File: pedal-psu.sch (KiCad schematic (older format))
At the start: 89 parts, among them J1 Conn_01x01_Male, J2 Conn_01x01_Male, J3 Power Sockets, J4 LCD Display, J7 Status LEDS, T1 Transformer_1P_1S, T2 Transformer_1P_1S, U1 LM7809_TO220, U2 LM324, U3 LM7809_TO220, U4 LM7805_TO220, U5 LM317_3PinPackage, U6 LM7809_TO220, U7 74HC595

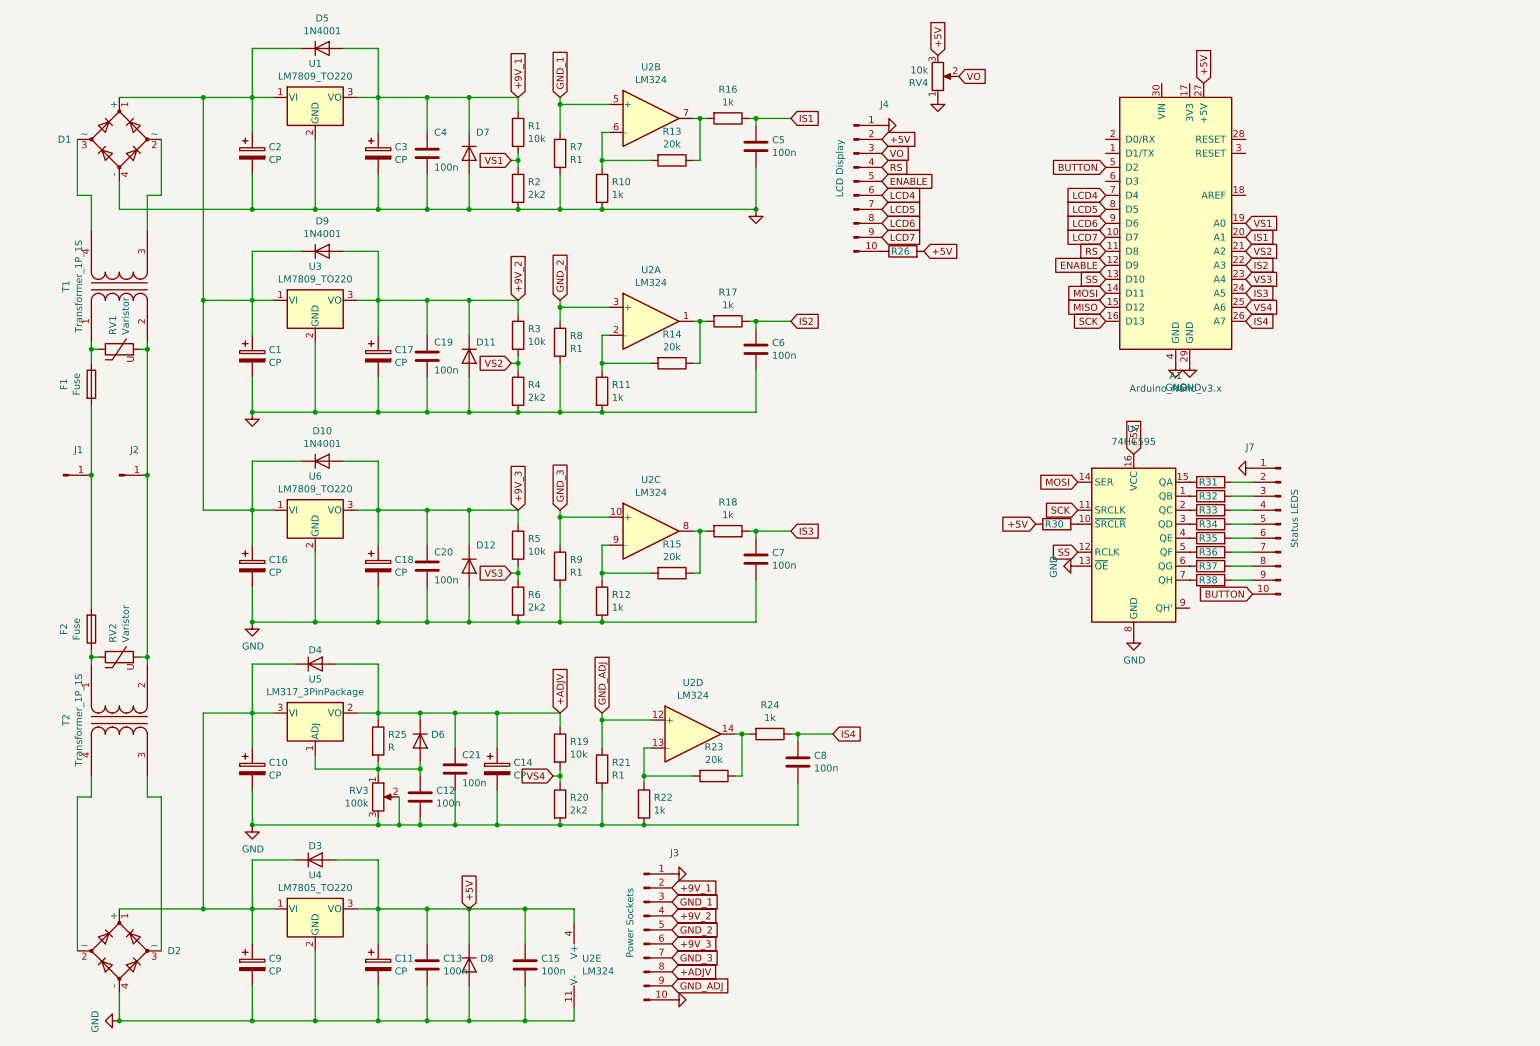
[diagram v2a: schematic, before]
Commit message: Removed 2nd trafo.
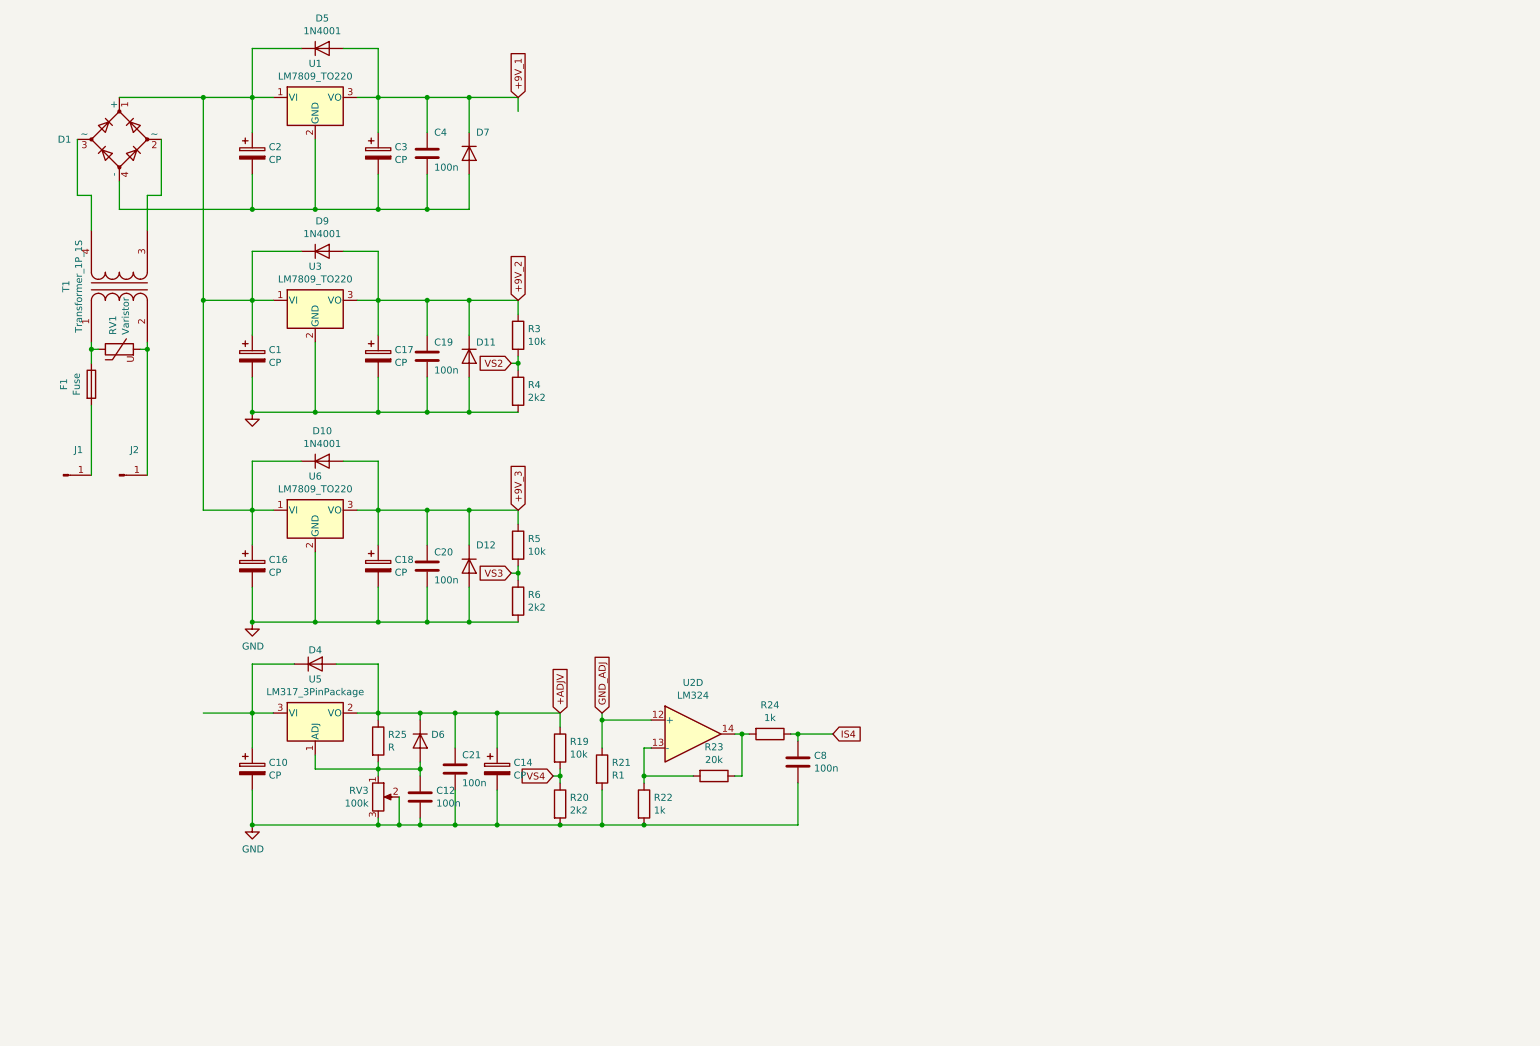
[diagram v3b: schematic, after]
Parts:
- removed A1: Arduino_Nano_v3.x, Module:Arduino_Nano, symbol MCU_Module:Arduino_Nano_v3.x
- removed C11: CP, Capacitor_THT:C_Radial_D6.3mm_H5.0mm_P2.50mm, symbol Device:CP
- removed C13, C15, C5, C6, C7: 100n, Capacitor_SMD:C_1210_3225Metric_Pad1.42x2.65mm_HandSolder, symbol Device:C
- removed C9: CP, Capacitor_THT:C_Radial_D10.0mm_H12.5mm_P5.00mm, symbol Device:CP
- removed D2: D_Bridge_+AA-, PartsStash:Diode_Bridge_TELPOD_GB009_p4mm, symbol Device:D_Bridge_+AA-
- removed D3, D8: 1N4001, Diode_SMD:D_SMA_Handsoldering, symbol Diode:1N4001
- removed F2: Fuse, PartsStash:Fuse-PTF15, symbol Device:Fuse
- removed J3: Power Sockets, Connector_Molex:Molex_KK-254_AE-6410-10A_1x10_P2.54mm_Vertical, symbol Connector:Conn_01x10_Male
- removed J4: LCD Display, Connector_Molex:Molex_KK-254_AE-6410-10A_1x10_P2.54mm_Vertical, symbol Connector:Conn_01x10_Male
- removed J7: Status LEDS, Connector_Molex:Molex_KK-254_AE-6410-10A_1x10_P2.54mm_Vertical, symbol Connector:Conn_01x10_Male
- removed R1: 10k, Resistor_SMD:R_0805_2012Metric_Pad1.15x1.40mm_HandSolder, symbol Device:R
- removed R10, R11, R12, R16, R17, R18: 1k, Resistor_SMD:R_0805_2012Metric_Pad1.15x1.40mm_HandSolder, symbol Device:R
- removed R13, R14, R15: 20k, Resistor_SMD:R_0805_2012Metric_Pad1.15x1.40mm_HandSolder, symbol Device:R
- removed R2: 2k2, Resistor_SMD:R_0805_2012Metric_Pad1.15x1.40mm_HandSolder, symbol Device:R
- removed R26: 220, Resistor_SMD:R_0805_2012Metric_Pad1.15x1.40mm_HandSolder, symbol Device:R
- removed R30: 100k, Resistor_SMD:R_0805_2012Metric_Pad1.15x1.40mm_HandSolder, symbol Device:R
- removed R31, R32, R33, R34, R35, R36, R37, R38: 560, Resistor_SMD:R_0805_2012Metric_Pad1.15x1.40mm_HandSolder, symbol Device:R
- removed R7, R8, R9: R1, Resistor_SMD:R_2512_6332Metric_Pad1.52x3.35mm_HandSolder, symbol Device:R
- removed RV2: Varistor, Varistor:RV_Disc_D15.5mm_W3.9mm_P7.5mm, symbol Device:Varistor
- removed RV4: 10k, Potentiometer_THT:Potentiometer_Piher_PT-6-V_Vertical, symbol Device:R_POT
- removed T2: Transformer_1P_1S, PartsStash:Transformer_V42AJ, symbol Device:Transformer_1P_1S
- removed unit 2 of U2
- removed unit 1 of U2
- removed unit 3 of U2
- removed unit 5 of U2
- removed U4: LM7805_TO220, PartsStash:TO220_Vertical_Radiator_L15mm_W10mm, symbol Regulator_Linear:LM7805_TO220
- removed U7: 74HC595, Package_SO:SOP-16_4.4x10.4mm_P1.27mm, symbol 74xx:74HC595
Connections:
- net GND: no longer C2.2, C3.2, C4.2, D1.4 (-), D7.2 (A), U1.2 (GND)
- new net: C2.2, C3.2, C4.2, D1.4 (-), D7.2 (A), U1.2 (GND)

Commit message: Complete PCB ready for hand etching.
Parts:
- removed R21: R1, Resistor_SMD:R_2512_6332Metric_Pad1.52x3.35mm_HandSolder, symbol Device:R
- removed R22, R24: 1k, Resistor_SMD:R_0805_2012Metric_Pad1.15x1.40mm_HandSolder, symbol Device:R
- removed R23: 20k, Resistor_SMD:R_0805_2012Metric_Pad1.15x1.40mm_HandSolder, symbol Device:R
- removed U2: LM324, Package_SO:SOIC-14_3.9x8.7mm_P1.27mm, symbol Amplifier_Operational:LM324
- added C13, C7: CP, Capacitor_THT:C_Radial_D6.3mm_H5.0mm_P2.50mm, symbol Device:CP
- added C14: 100n, Capacitor_SMD:C_1210_3225Metric_Pad1.42x2.65mm_HandSolder, symbol Device:C
- added D11, D3, D6, D9: 1N4001, Diode_THT:D_DO-41_SOD81_P7.62mm_Horizontal, symbol Diode:1N4001
- added J3, J4, J5, J6, J7, J8: Conn_01x02_Male, Connector_Molex:Molex_KK-254_AE-6410-02A_1x02_P2.54mm_Vertical, symbol Connector:Conn_01x02_Male
- added R10, R11, R12, R8, R9: 1k, Resistor_SMD:R_0805_2012Metric_Pad1.15x1.40mm_HandSolder, symbol Device:R
- added R13: 3k9, Resistor_SMD:R_0805_2012Metric_Pad1.15x1.40mm_HandSolder, symbol Device:R
- added R14: 100R, Resistor_SMD:R_0805_2012Metric_Pad1.15x1.40mm_HandSolder, symbol Device:R
- added R15, R16, R17, R18: 470R, Resistor_SMD:R_0805_2012Metric_Pad1.15x1.40mm_HandSolder, symbol Device:R
- added R2: 470, Resistor_SMD:R_0805_2012Metric_Pad1.15x1.40mm_HandSolder, symbol Device:R
- added R7: 1k2, Resistor_SMD:R_0805_2012Metric_Pad1.15x1.40mm_HandSolder, symbol Device:R
- added RV3: 2K, Connector_Molex:Molex_KK-254_AE-6410-03A_1x03_P2.54mm_Vertical, symbol Device:R_POT
- added U2: LM78L09, Package_TO_SOT_THT:TO-92, symbol Regulator_Linear:L78L09_TO92
- added U5: LM7809_TO220, PartsStash:TO220_Vertical_Radiator_L15mm_W10mm, symbol Regulator_Linear:LM7809_TO220
- added U7, U8, U9: LM358, Package_SO:SOIC-8_3.9x4.9mm_P1.27mm, symbol Amplifier_Operational:LM358
- D10: renamed from D7; footprint Diode_SMD:D_SMA_Handsoldering -> Diode_THT:D_DO-41_SOD81_P7.62mm_Horizontal
- D12: renamed from D4; footprint Diode_SMD:D_SMA_Handsoldering -> Diode_THT:D_DO-41_SOD81_P7.62mm_Horizontal
- D13: renamed from D6; footprint Diode_SMD:D_SMA_Handsoldering -> Diode_THT:D_DO-41_SOD81_P7.62mm_Horizontal
- D2: renamed from D10; footprint Diode_SMD:D_SMA_Handsoldering -> Diode_THT:D_DO-41_SOD81_P7.62mm_Horizontal
- D4: renamed from D9; footprint Diode_SMD:D_SMA_Handsoldering -> Diode_THT:D_DO-41_SOD81_P7.62mm_Horizontal
- D5: renamed from D12; footprint Diode_SMD:D_SMA_Handsoldering -> Diode_THT:D_DO-41_SOD81_P7.62mm_Horizontal
- D7: renamed from D11; footprint Diode_SMD:D_SMA_Handsoldering -> Diode_THT:D_DO-41_SOD81_P7.62mm_Horizontal
- D8: renamed from D5; footprint Diode_SMD:D_SMA_Handsoldering -> Diode_THT:D_DO-41_SOD81_P7.62mm_Horizontal
- R1: renamed from R25; value R -> 270
- R19: value 10k -> 470R
- R20: value 2k2 -> 470R
- R3: value 10k -> 22k
- R4: value 2k2 -> 22k
- R5: value 10k -> 3k9
- R6: value 2k2 -> 3k9
- RV2: renamed from RV3; value 100k -> 1K
- U1: renamed from U6; value LM7809_TO220 -> LM78L09; footprint PartsStash:TO220_Vertical_Radiator_L15mm_W10mm -> Package_TO_SOT_THT:TO-92; symbol Regulator_Linear:LM7809_TO220 -> Regulator_Linear:L78L09_TO92
- U3: value LM7809_TO220 -> LM78L09; footprint PartsStash:TO220_Vertical_Radiator_L15mm_W10mm -> Package_TO_SOT_THT:TO-92; symbol Regulator_Linear:LM7809_TO220 -> Regulator_Linear:L78L09_TO92
- U4: renamed from U1; value LM7809_TO220 -> LM78L09; footprint PartsStash:TO220_Vertical_Radiator_L15mm_W10mm -> Package_TO_SOT_THT:TO-92; symbol Regulator_Linear:LM7809_TO220 -> Regulator_Linear:L78L09_TO92
- renumbered C19 to C10, C3 to C11, C4 to C12, C12 to C15, C21 to C16, C14 to C17, C16 to C3, C10 to C4, C18 to C5, C20 to C6, C17 to C9, U5 to U6
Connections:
- net +9V_1: now also U4.1 (VO), J6.1 (Pin_1); no longer U4.3 (VO)
- net +9V_2: now also U3.1 (VO), J5.1 (Pin_1); no longer R3.1, U3.3 (VO)
- net +9V_3: now also U1.1 (VO), J3.1 (Pin_1); no longer R5.1, U1.3 (VO)
- net +ADJV: now also R3.1, J7.1 (Pin_1), RV3.1, RV3.2; no longer C16.1, C17.1, D12.2 (A), D13.1 (K), R1.1, R19.1, U6.2 (VO)
- net GND: now also C11.2, C12.2, C2.2, D1.4 (-), D10.2 (A), U4.2 (GND), C13.2, C14.2, C7.2, D11.2 (A), D6.2 (A), J3.2 (Pin_2), J4.2 (Pin_2), J5.2 (Pin_2), J6.2 (Pin_2), J7.2 (Pin_2), J8.2 (Pin_2), R14.2, U2.2 (GND), U5.2 (GND), U7.4 (V-), U8.4 (V-), U9.4 (V-); no longer R20.2, R6.2
- net +12V: now reaches C1.1, C2.1, C3.1, D1.1 (+), D2.1 (K), D4.1 (K), D8.1 (K)
- net +12V: now also C4.1, D12.1 (K), U1.3 (VI), U3.3 (VI), U4.3 (VI), U6.3 (VI), D3.1 (K), D9.1 (K), U2.3 (VI), U5.1 (VI); no longer U1.1 (VI), U3.1 (VI), U4.1 (VI)
- net at C15.1, D13.2 (A), R1.2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: now also R2.1; no longer RV2.1
- net IS4 renamed +9V_4
- net +9V_4: now also C7.1, D3.2 (A), D6.1 (K), J4.1 (Pin_1), U2.1 (VO)
- net VS2 renamed V_SENSE
- net V_SENSE: now also U7.3 (+), U7.5 (+), U8.3 (+), U8.5 (+), U9.3 (+), U9.5 (+)
- net VS3: no longer names the net of R5.2, R6.1
- net VS4: no longer names the net of R20.1
- net VS4: now also U7.1; no longer R19.2
- new net: R2.2, RV2.1
- new net: R6.2, R7.1
- new net: R7.2, R8.1, U9.2 (-)
- new net: R8.2, R9.1, U9.6 (-)
- new net: R10.1, R9.2, U8.2 (-)
- new net: R10.2, R11.1, U8.6 (-)
- new net: R11.2, R12.1, U7.2 (-)
- new net: R12.2, R13.1, U7.6 (-)
- new net: R13.2, R14.1
- new net: R19.1, U7.7
- new net: R18.1, U8.1
- new net: R17.1, U8.7
- new net: R16.1, U9.1
- new net: R15.1, U9.7
- new net +9V_5: C13.1, C14.1, D11.1 (K), D9.2 (A), J8.1 (Pin_1), R5.1, U5.3 (VO), U7.8 (V+), U8.8 (V+), U9.8 (V+)
- new net ADJ: C16.1, C17.1, D12.2 (A), D13.1 (K), R1.1, RV3.3, U6.2 (VO)
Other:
- moved on the sheet: C1, C10, C11, C12, C15, C16, C17, C2, C3, C4, C5, C6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
